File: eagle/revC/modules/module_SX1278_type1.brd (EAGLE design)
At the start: 24.1 x 32.8 mm, 17 parts, among them X1 734120110

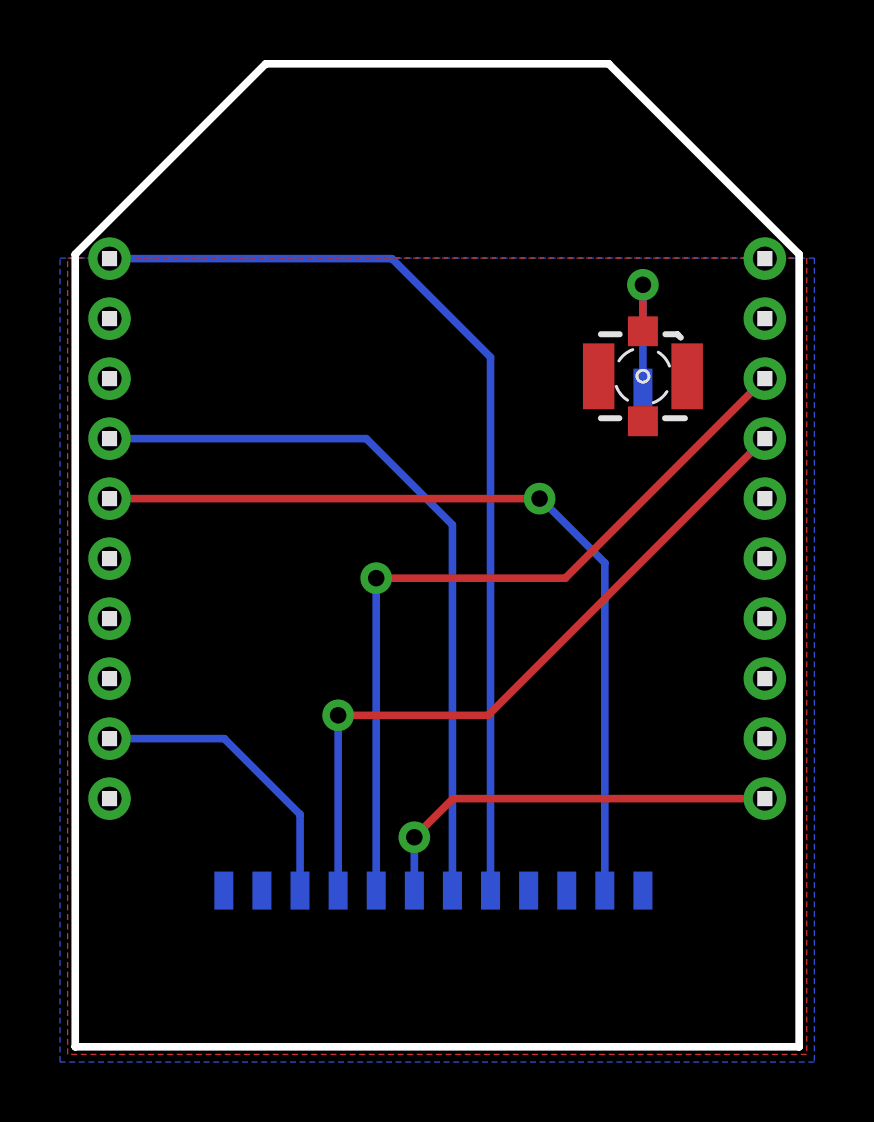
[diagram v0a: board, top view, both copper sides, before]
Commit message: Replaced modules with library parts
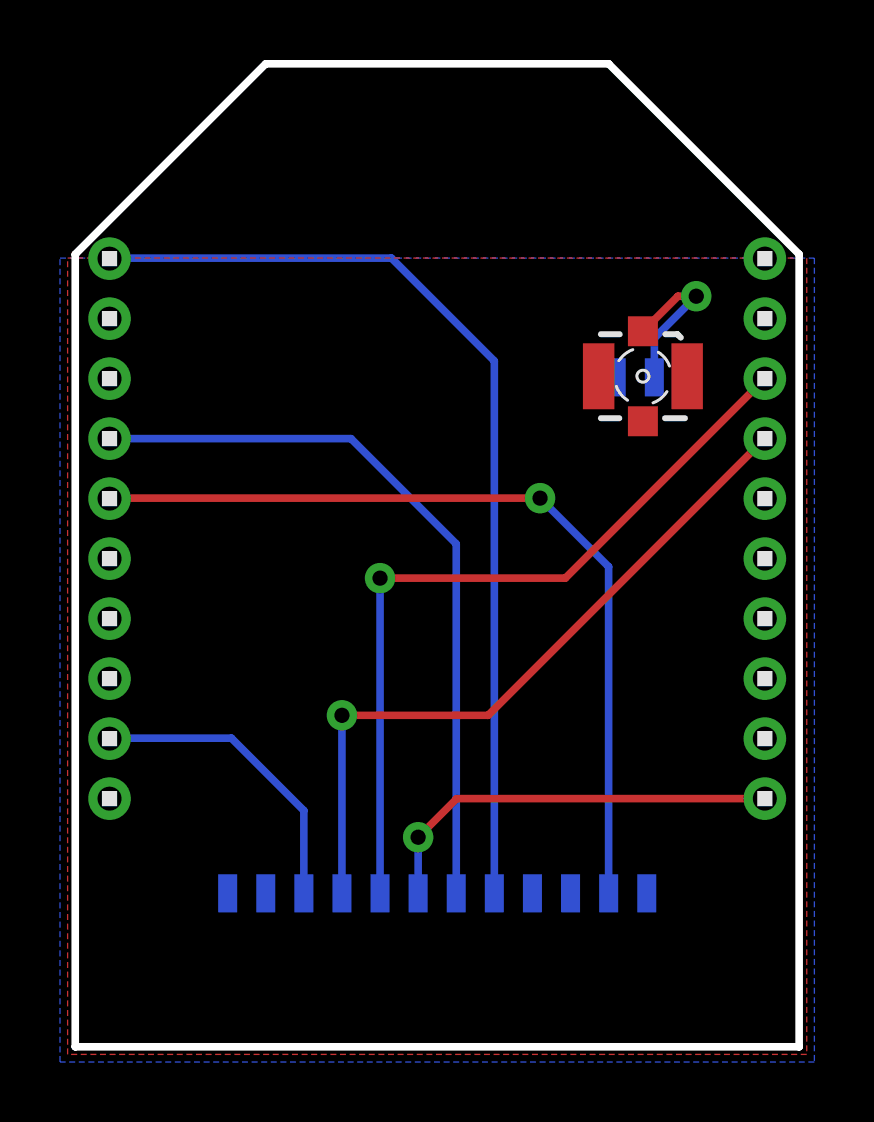
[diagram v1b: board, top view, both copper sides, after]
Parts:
- removed ANT, DIO0, DIO1, DIO2, DIO3, GND, GND2, GND_ANT, MISO, MOSI, NSS, RESET, SLCK, VCC: (no value), wirepad:SMD0,65-1,27
- added U$1: SX1278_1, RadioShield:SX1278_1
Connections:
- removed net ANT: ANT.1, X1.1
- removed net INT0: DIO0.1, LEFT1.9
- removed net INT1: DIO1.1, LEFT1.5
- removed net SPI_CS: NSS.1, RIGHT1.4
- removed net SPI_MISO: LEFT1.4, MISO.1
- removed net SPI_MOSI: MOSI.1, RIGHT1.10
- removed net SPI_SCK: RIGHT1.3, SLCK.1
- removed net VCC: LEFT1.1, VCC.1
- new net N$1: U$1.ANT, X1.1
- new net N$2: RIGHT1.10, U$1.MOSI
- new net N$3: RIGHT1.4, U$1.NSS
- new net N$4: RIGHT1.3, U$1.SCK
- new net N$5: LEFT1.9, U$1.DIO0
- new net N$6: LEFT1.5, U$1.DIO1
- new net N$7: LEFT1.4, U$1.MISO
- new net N$8: LEFT1.1, U$1.VCC
- net GND: now also U$1.GND@1, U$1.GND@2, U$1.GND@3; no longer GND.1, GND2.1, GND_ANT.1
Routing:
- net N$8: track 0.00 -> 32.0 mm
- net VCC: track 31.8 -> 0.00 mm
- net N$6: track 0.00 -> 28.5 mm, vias 0 -> 1
- net INT1: track 28.3 -> 0.00 mm, vias 1 -> 0
- net SPI_SCK: track 26.1 -> 0.00 mm, vias 1 -> 0
- net N$4: track 0.00 -> 26.1 mm, vias 0 -> 1
- net SPI_MISO: track 24.8 -> 0.00 mm
- net N$7: track 0.00 -> 24.7 mm
- net SPI_CS: track 24.1 -> 0.00 mm, vias 1 -> 0
- net N$3: track 0.00 -> 23.9 mm, vias 0 -> 1
- net SPI_MOSI: track 14.0 -> 0.00 mm, vias 1 -> 0
- net N$2: track 0.00 -> 14.0 mm, vias 0 -> 1
- net N$5: track 0.00 -> 10.2 mm
- net INT0: track 9.94 -> 0.00 mm
- net N$1: track 0.00 -> 5.54 mm, vias 0 -> 1
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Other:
- board text removed: "ANT"
- board text removed: "DIO0"
- board text removed: "DIO1"
- board text removed: "DIO2"
- board text removed: "DIO3"
- board text removed: "GND"
- board text removed: "MISO"
- board text removed: "MOSI"
- board text removed: "NSS"
- board text removed: "RESET"
- board text removed: "SLCK"
- board text removed: "VCC"

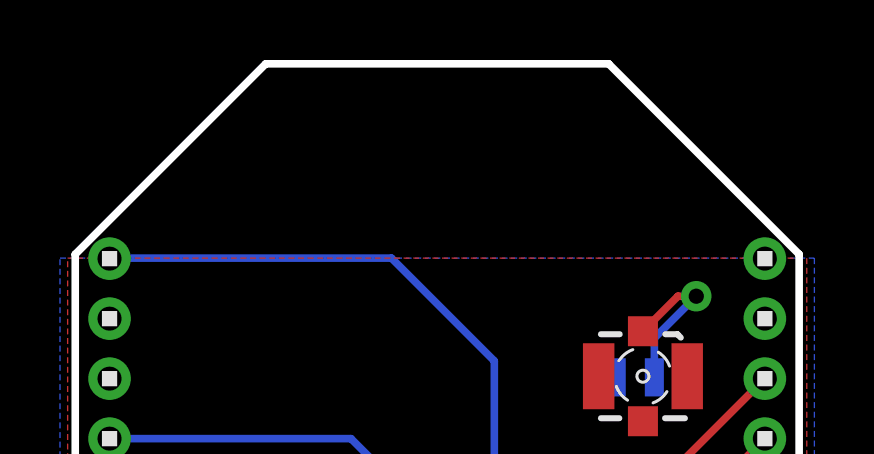
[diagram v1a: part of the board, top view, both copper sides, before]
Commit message: Fixed module name layers
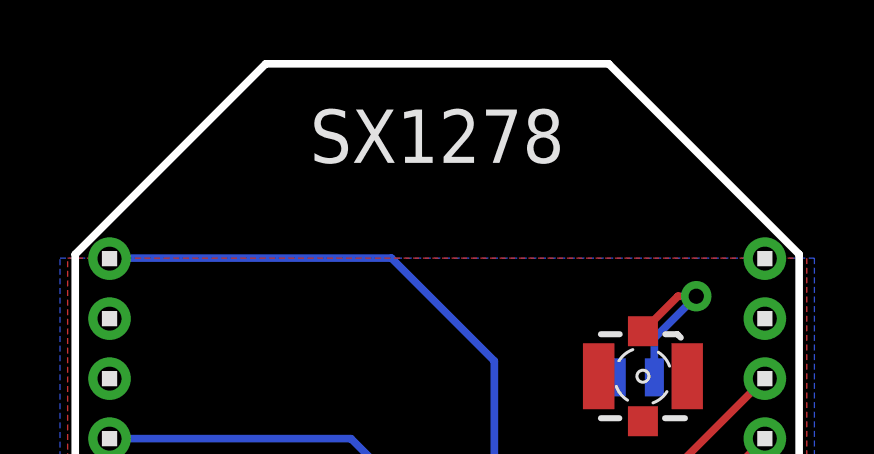
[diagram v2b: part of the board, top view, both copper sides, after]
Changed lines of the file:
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@@
 <wire x1="24.257" y1="26.543" x2="24.257" y2="0.127" width="0.254" layer="20"/>
 <wire x1="24.257" y1="0.127" x2="0.127" y2="0.127" width="0.254" layer="20"/>
-<text x="12.192" y="30.48" size="1.778" layer="51" ratio="15" rot="SR0" align="center">SX1278</text>
+<text x="12.192" y="30.48" size="1.778" layer="25" ratio="15" rot="SR0" align="center">SX1278</text>
 </plain>
 <attributes>
